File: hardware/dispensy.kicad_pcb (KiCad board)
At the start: 2 copper layers, 125 x 90 mm, 96 parts, among them SW1 BOOTSEL, SW2 RESET, SW3 UP, SW4 MENU, SW5 DOWN, U1 DBT50G-7_62-4P, U10 RP2040, U11 SS54_C22452, U12 SS54_C22452, U13 CAN_IO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

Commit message: nearly done with routing
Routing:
- net GND: track 774.5 -> 799.9 mm, vias 17 -> 21
- net +3.3V: track 290.7 -> 307.3 mm
- net /PI/IO13: track 80.5 -> 81.4 mm
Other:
- board text added: "V1"

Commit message: route more gnd
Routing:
- net GND: track 799.9 -> 816.7 mm, vias 21 -> 22
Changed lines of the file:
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@@
   (title_block
     (title "Dispensy Mainboard")
-    (date "2024-02-10")
+    (date "2024-03-04")
     (rev "1")
     (company "DrinkRobotics")
@@
   (segment (start 139.820167 108.34763) (end 140.275082 107.892715) (width 0.5) (layer "F.Cu") (net 1))
   (segment (start 107.717773 67.717773) (end 110.5 70.5) (width 2) (layer "F.Cu") (net 1))
+  (segment (start 122.775082 114.019969) (end 124.019969 114.019969) (width 0.5) (layer "F.Cu") (net 1))
   (segment (start 129.010667 122.937546) (end 129.010667 121.667544) (width 0.5) (layer "F.Cu") (net 1))
   (segment (start 145.034925 78.549975) (end 145.034925 73.034925) (width 1) (layer "F.Cu") (net 1))
@@
   (segment (start 191.329819 106.787827) (end 191.709881 106.407765) (width 0.5) (layer "F.Cu") (net 1))
   (segment (start 169.882887 58.51762) (end 172.382887 61.01762) (width 1) (layer "F.Cu") (net 1))
+  (segment (start 124.019969 114.019969) (end 124.5 114.5) (width 0.5) (layer "F.Cu") (net 1))
   (segment (start 191.334849 94.487648) (end 191.754966 94.487648) (width 0.5) (layer "F.Cu") (net 1))
   (segment (start 140.8349 83.049975) (end 144.484925 83.049975) (width 1) (layer "F.Cu") (net 1))
@@
   (via (at 142 129.5) (size 1) (drill 0.5) (layers "F.Cu" "B.Cu") (net 1))
   (via (at 143.5 73) (size 1) (drill 0.5) (layers "F.Cu" "B.Cu") (net 1))
+  (via (at 124.5 114.5) (size 0.5) (drill 0.2) (layers "F.Cu" "B.Cu") (net 1))
   (segment (start 135 75) (end 135 86) (width 2) (layer "B.Cu") (net 1))
   (segment (start 204.254966 94.847154) (end 202.625458 93.217646) (width 0.5) (layer "B.Cu") (net 1))
@@
   (segment (start 121.275082 126.03813) (end 121 126.313212) (width 0.5) (layer "B.Cu") (net 1))
   (segment (start 101.282227 67.717773) (end 99.5 69.5) (width 2) (layer "B.Cu") (net 1))
-  (segment (start 125.5 101.5) (end 127.5 101.5) (width 0.5) (layer "B.Cu") (net 1))
   (segment (start 143.5 73) (end 145 73) (width 2) (layer "B.Cu") (net 1))
   (segment (start 144.5 99.5) (end 138 99.5) (width 0.5) (layer "B.Cu") (net 1))
@@
   (segment (start 187.189992 57.5) (end 179.569977 57.5) (width 2) (layer "B.Cu") (net 1))
   (segment (start 187.189992 57.5) (end 191.189992 53.5) (width 1) (layer "B.Cu") (net 1))
+  (segment (start 126.5 101.5) (end 126.5 99.5) (width 0.5) (layer "B.Cu") (net 1))
+  (segment (start 124.5 114.5) (end 124.5 108) (width 0.5) (layer "B.Cu") (net 1))
   (segment (start 179.569977 60.01811) (end 179.569977 57.5) (width 2) (layer "B.Cu") (net 1))
   (segment (start 109.5 98.689992) (end 102.810008 98.689992) (width 2) (layer "B.Cu") (net 1))
@@
   (segment (start 130.5 95.5) (end 131 96) (width 2) (layer "B.Cu") (net 1))
   (segment (start 156.5 134) (end 159 134) (width 0.5) (layer "B.Cu") (net 1))
+  (segment (start 126.5 101.5) (end 127.5 101.5) (width 0.5) (layer "B.Cu") (net 1))
   (segment (start 202.625458 84.327628) (end 203.835103 84.327628) (width 0.5) (layer "B.Cu") (net 1))
   (segment (start 131 96) (end 134.5 96) (width 2) (layer "B.Cu") (net 1))
@@
   (segment (start 155 132.5) (end 156.5 134) (width 0.5) (layer "B.Cu") (net 1))
   (segment (start 201.355454 79.247618) (end 200.085452 80.51762) (width 0.5) (layer "B.Cu") (net 1))
+  (segment (start 126.5 99.5) (end 130.5 95.5) (width 0.5) (layer "B.Cu") (net 1))
   (segment (start 127.5 101.5) (end 128 102) (width 0.5) (layer "B.Cu") (net 1))
   (segment (start 205.189992 53.5) (end 207.189992 55.5) (width 1) (layer "B.Cu") (net 1))
@@
   (segment (start 128 102) (end 128 103) (width 0.5) (layer "B.Cu") (net 1))
   (segment (start 102.5 126) (end 109 132.5) (width 2) (layer "B.Cu") (net 1))
+  (segment (start 124.5 108) (end 124 107.5) (width 0.5) (layer "B.Cu") (net 1))
   (segment (start 204.254966 80.877126) (end 202.625458 79.247618) (width 0.5) (layer "B.Cu") (net 1))
   (segment (start 203.835103 84.327628) (end 204.254966 83.907765) (width 0.5) (layer "B.Cu") (net 1))
   (segment (start 143 73) (end 143.5 73) (width 2) (layer "B.Cu") (net 1))
+  (segment (start 125.5 101.5) (end 126.5 101.5) (width 0.5) (layer "B.Cu") (net 1))
   (segment (start 137 73) (end 135 75) (width 2) (layer "B.Cu") (net 1))
   (segment (start 142 129.5) (end 142 128) (width 2) (layer "B.Cu") (net 1))

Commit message: nearly done with routing, one track missing
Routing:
- net +3.3V: track 307.3 -> 362.4 mm
- net +1V1: track 19.6 -> 29.5 mm, vias 0 -> 2
- net GND: track 816.7 -> 816.0 mm

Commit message: no unrouted tracks left
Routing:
- net +1V1: track 29.5 -> 38.5 mm, vias 2 -> 3
- net +3.3V: track 362.4 -> 371.0 mm, vias 11 -> 13

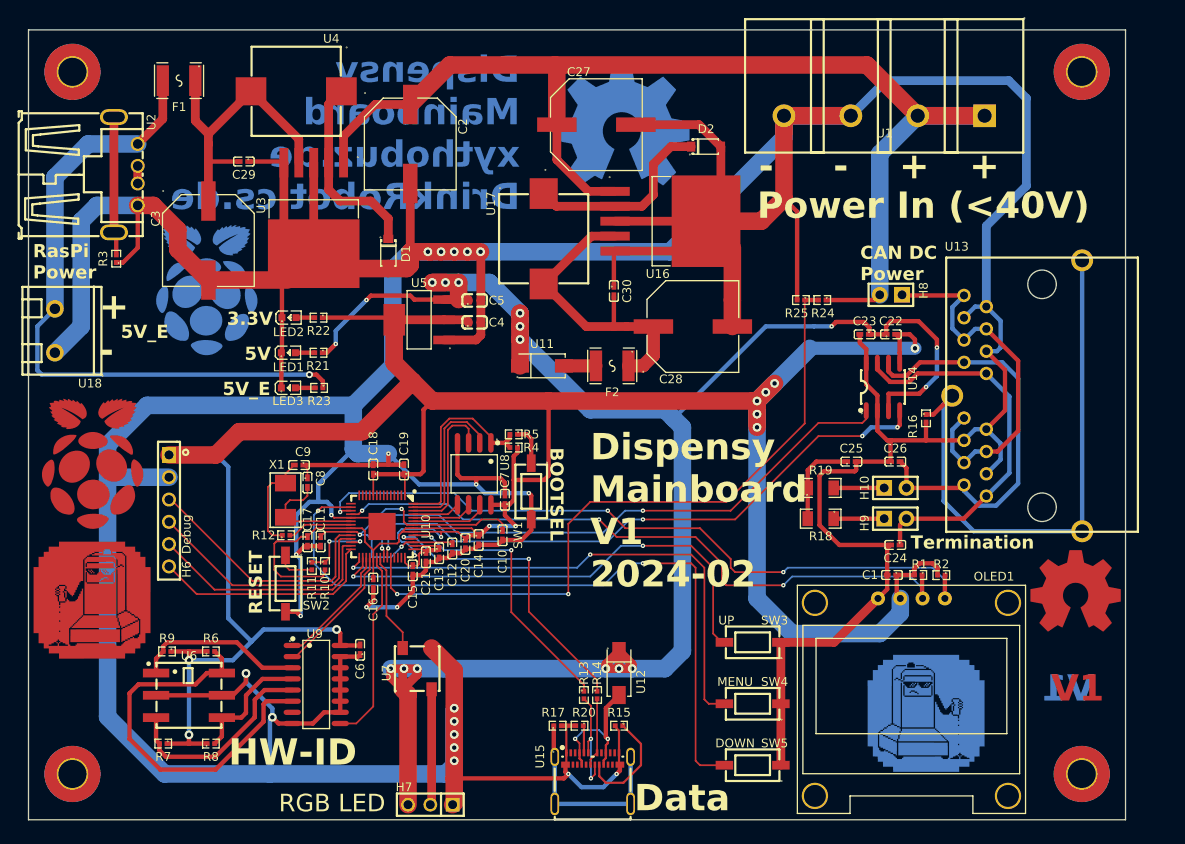
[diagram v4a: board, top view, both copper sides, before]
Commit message: add ground planes
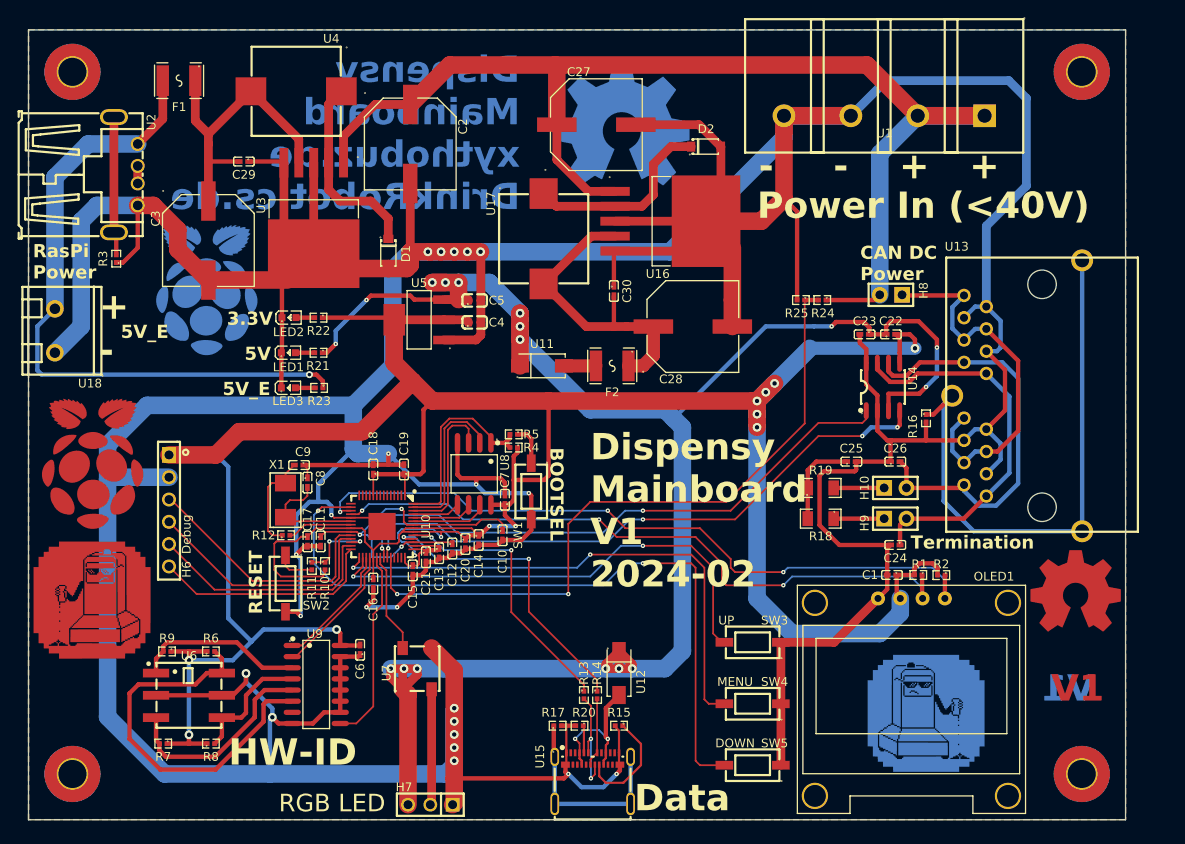
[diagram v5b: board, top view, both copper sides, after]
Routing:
- added copper zone on B.Cu, net GND
- added copper zone on F.Cu, net GND
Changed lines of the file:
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@@
   (segment (start 126.169164 88.506858) (end 123.904877 88.506858) (width 0.5) (layer "F.Cu") (net 91))
   (segment (start 123.904877 88.506858) (end 123.901448 88.503429) (width 0.5) (layer "F.Cu") (net 91))
+  (zone (net 1) (net_name "GND") (layers "F&B.Cu") (hatch edge 0.5)
+    (connect_pads (clearance 0.5))
+    (min_thickness 0.25) (filled_areas_thickness no)
+    (fill yes (thermal_gap 0.5) (thermal_bridge_width 0.5))
+    (polygon
+      (pts
+        (xy 93.5 47.7)
+        (xy 218.5 47.7)
+        (xy 218.5 137.7)
+        (xy 93.5 137.7)
+      )
+    )
+  )
   (group "" (id 33974a4d-45b5-4390-9e64-4750a52007ea)
     (members
